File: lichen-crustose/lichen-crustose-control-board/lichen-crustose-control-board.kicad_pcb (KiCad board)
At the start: 4 copper layers, 48 x 108 mm, 77 parts, among them J1 Thonkiconn_Mono_Audio_Jack, J2 Thonkiconn_Mono_Audio_Jack, J3 Thonkiconn_Mono_Audio_Jack, J4 Thonkiconn_Mono_Audio_Jack, J5 Thonkiconn_Mono_Audio_Jack, J6 Thonkiconn_Mono_Audio_Jack, J7 Thonkiconn_Mono_Audio_Jack, J8 Thonkiconn_Mono_Audio_Jack, U1 NSL-32SR3, U2 NS-32SR2

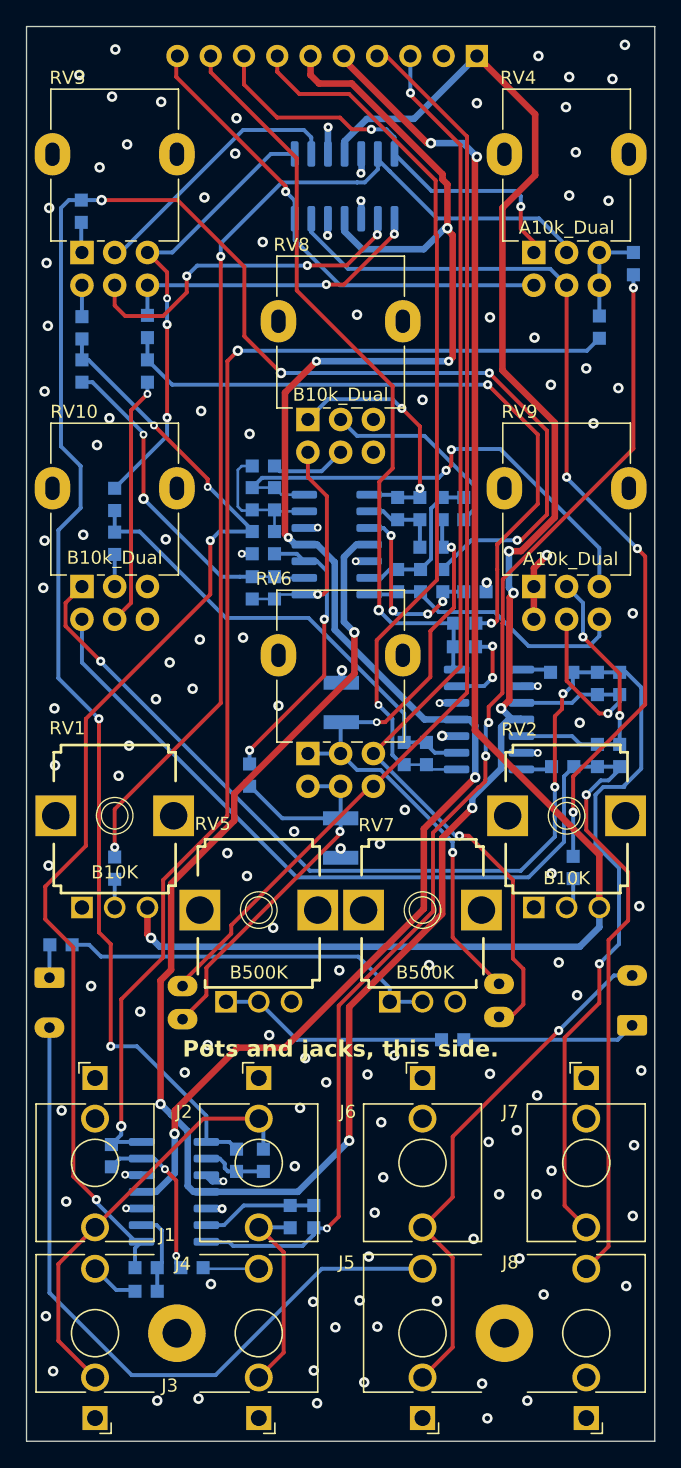
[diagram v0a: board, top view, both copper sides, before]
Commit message: Updates Lichen symbols and footprints. Fixes to Crustose and Vactrol VCA. Adds 3D model of the RP2350 dual USB board.
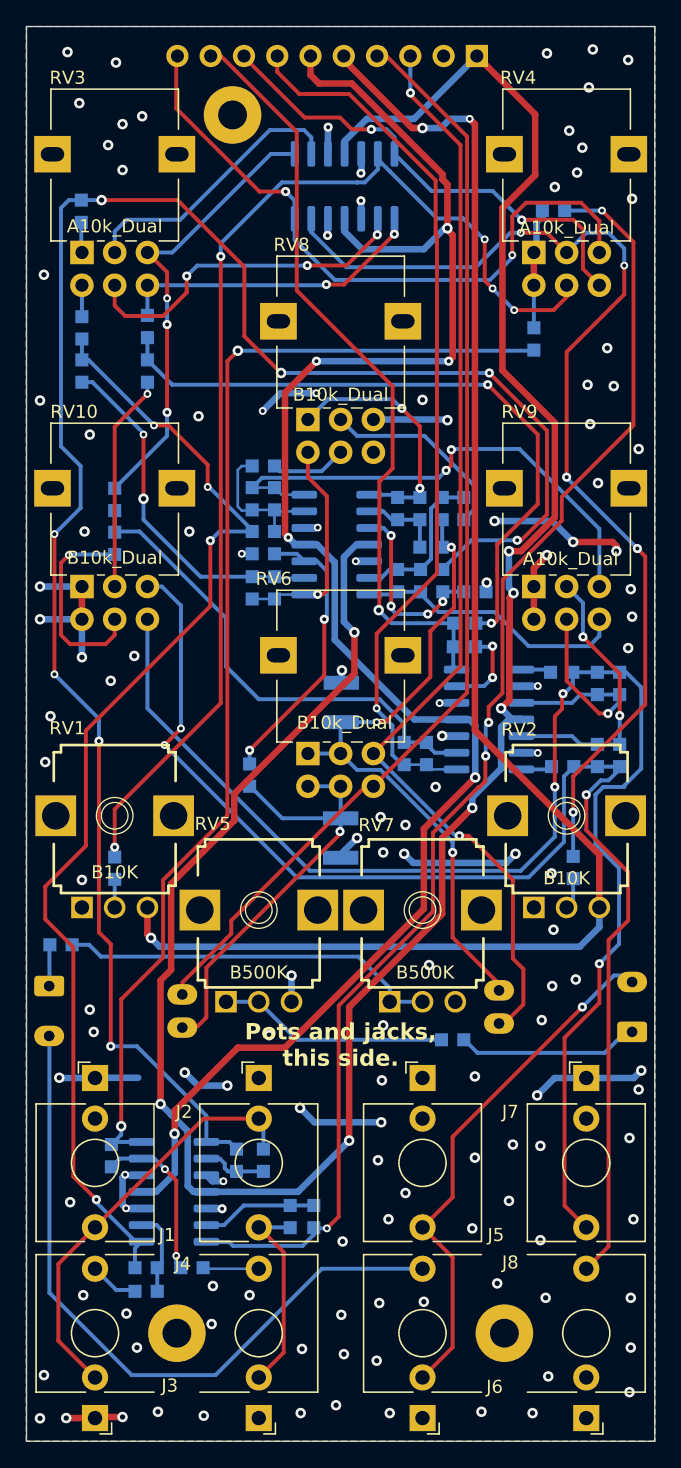
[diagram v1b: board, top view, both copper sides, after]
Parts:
- added H3: MountingHole_Pad, MountingHole:MountingHole_2.2mm_M2_Pad, F.Cu at (117.0, 117.0)
- R10, R13, R14: value 4.7k_0603 -> 5.1k_0603
- R11, R12, R35, R36, R37, R38, R39, R40: value 100k_0603 -> 10k_0603
- R15, R16, R33, R34: value 10k_0603 -> 1k_0603
- moved R13 7.32 mm to (141.5, 124.3), turned to 180 degrees
- moved R14 5.08 mm to (140.0, 134.1)
- moved U2 0.64 mm to (103.0, 183.5)
- moved U1 0.50 mm to (147.5, 187.0)
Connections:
- RV10 pad 1: /OUTPUT_FEEDBACK_L -> GND
- RV10 pad 2: /Amplifiers/FEEDBACK_MIX_L -> /Amplifiers/FEEDBACK_MIX_R
- RV10 pad 3: GND -> /OUTPUT_FEEDBACK_R
- RV10 pad 4: /OUTPUT_FEEDBACK_R -> GND
- RV10 pad 5: /Amplifiers/FEEDBACK_MIX_R -> /Amplifiers/FEEDBACK_MIX_L
- RV10 pad 6: GND -> /OUTPUT_FEEDBACK_L
- RV4 pad 1: /CARRER_CONNECTOR_L -> /Amplifiers/CARRIER_UNAMPLIFIED_L
- RV4 pad 2: /Amplifiers/CARRIER_AMPLIFICATION_L -> /Amplifiers/CARRER_AMPLIFICATION_R
- RV4 pad 3: /Amplifiers/CARRIER_UNAMPLIFIED_L -> /PROGRAM_CONNECTOR_R
- RV4 pad 4: /PROGRAM_CONNECTOR_R -> /Amplifiers/CARRIER_UNAMPLIFIED_L
- RV4 pad 5: /Amplifiers/CARRER_AMPLIFICATION_R -> /Amplifiers/CARRIER_AMPLIFICATION_L
- RV4 pad 6: /Amplifiers/CARRIER_UNAMPLIFIED_L -> /CARRER_CONNECTOR_L
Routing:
- net GND: track 26.9 -> 104.1 mm, vias 130 -> 134
- net /Amplifiers/FEEDBACK_MIX_L: track 2.45 -> 15.7 mm, vias 0 -> 1
- net /PROGRAM_CONNECTOR_R: track 37.5 -> 50.8 mm, vias 1 -> 2
- net /Amplifiers/CARRER_AMPLIFICATION_R: track 70.6 -> 81.8 mm, vias 3 -> 5
- net /Amplifiers/CARRIER_IN_L: track 92.8 -> 101.5 mm
- net /OUTPUT_FEEDBACK_L: track 115.6 -> 110.0 mm, vias 4 -> 3
- net /Amplifiers/CARRIER_IN_R: track 95.0 -> 89.6 mm
- net /Amplifiers/CARRIER_AMPLIFICATION_L: track 83.8 -> 88.5 mm, vias 2 -> 5
- net /CARRER_CONNECTOR_L: track 32.3 -> 36.9 mm
- net /Amplifiers/FEEDBACK_MIX_R: track 19.1 -> 16.6 mm
- net /OUTPUT_FEEDBACK_R: track 100.0 -> 102.2 mm, vias 1 -> 3
- net -2.5V: track 113.9 -> 115.7 mm
- net /Amplifiers/CARRIER_UNAMPLIFIED_L: track 7.45 -> 9.22 mm
- net Net-(OP4C--): track 36.1 -> 37.9 mm
- net /Crossfaders/FILTER_OUT_R: track 33.2 -> 34.5 mm
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- added copper zone on B.Cu, net GND
- added copper zone on F.Cu, net GND
- removed copper zone on In1.Cu, net GND
- removed copper zone on In2.Cu, net GND
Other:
- copper layers 4 -> 2
- board text added: "v1.1 © 2026, Colin Clark"
- board text removed: "v1.0 © 2025, Colin Clark"

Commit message: feat: Updates Crustose, Cladonia and YouMe Transformer. Adds Stereo Latencies.
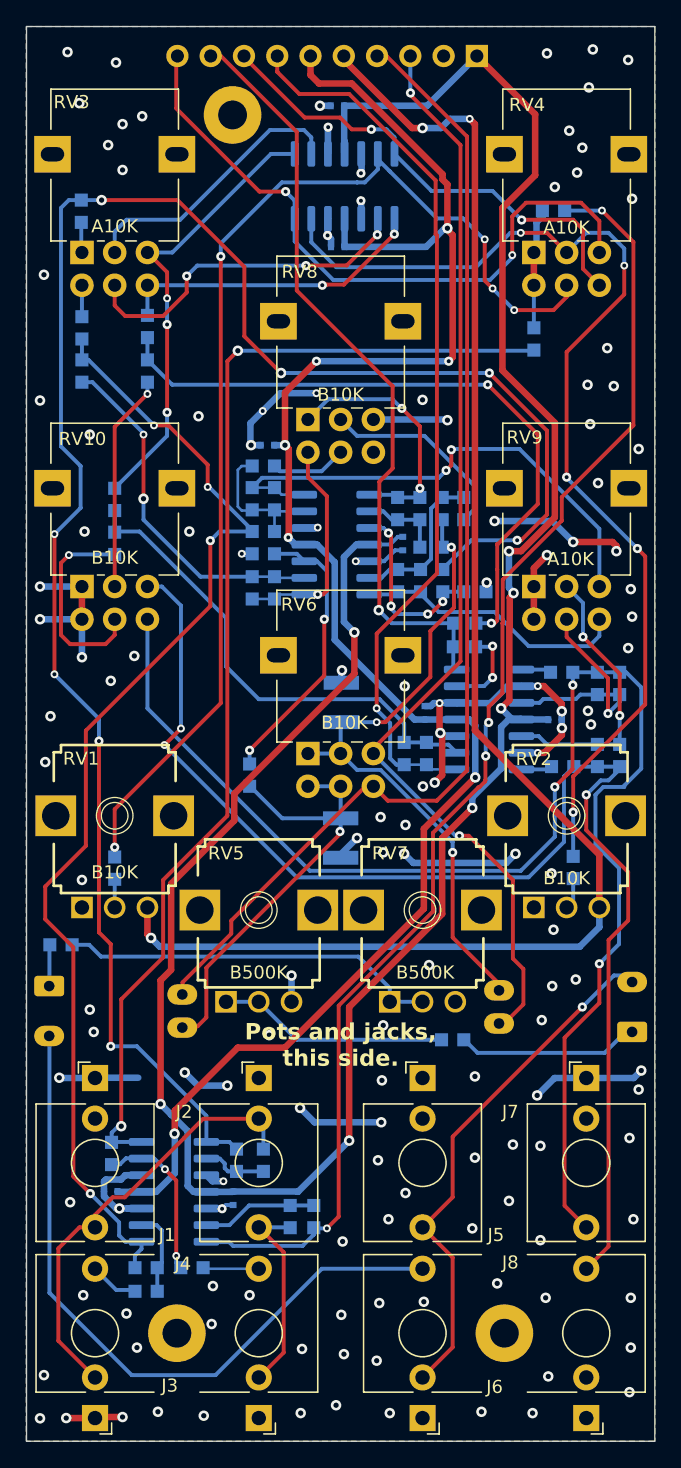
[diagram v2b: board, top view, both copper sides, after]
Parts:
- added C11: 100nF, RP2350_60QFN_minimal:C_0402_1005Metric_small_pads, B.Cu at (125.0, 116.3)
- added C12: 100nF, RP2350_60QFN_minimal:C_0402_1005Metric_small_pads, B.Cu at (141.6, 163.2)
- added C13: 100nF, RP2350_60QFN_minimal:C_0402_1005Metric_small_pads, B.Cu at (130.0, 149.7)
- added C14: 100nF, RP2350_60QFN_minimal:C_0402_1005Metric_small_pads, B.Cu at (117.0, 199.7)
- added C16: 100nF, RP2350_60QFN_minimal:C_0402_1005Metric_small_pads, B.Cu at (119.7, 142.2)
- added C17: 100nF, RP2350_60QFN_minimal:C_0402_1005Metric_small_pads, B.Cu at (107.7, 199.2)
- added C18: 100nF, RP2350_60QFN_minimal:C_0402_1005Metric_small_pads, B.Cu at (131.7, 162.6)
- added C19: 100nF, RP2350_60QFN_minimal:C_0402_1005Metric_small_pads, B.Cu at (125.0, 127.1)
- C3, C4, C5, C6: value 33pF_C0G_0603_50V -> 33pF C0G
- R1, R17, R18, R19, R2, R20, R21, R22, R23, R24, R25, R26, R27, R28, R29, R3, R30, R4, R5, R6, R7, R8: value 100k_0603 -> 100K
- R10, R13, R14, R9: value 5.1k_0603 -> 5.1K
- R11, R12, R31, R32, R35, R36, R37, R38, R39, R40: value 10k_0603 -> 10K
- R15, R16, R33, R34: value 1k_0603 -> 1K
- RV10, RV6, RV8: value B10k_Dual -> B10K
- RV3, RV4, RV9: value A10k_Dual -> A10K
- moved R8 0.17 mm to (107.8, 196.3)
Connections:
- net /Amplifiers/CARRER_AMPLIFICATION_R renamed /Amplifiers/CARRIER_OFFSET_R
- net /Amplifiers/CARRIER_AMPLIFICATION_L renamed /Amplifiers/CARRIER_OFFSET_L
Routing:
- net GND: track 104.1 -> 137.3 mm, vias 134 -> 141
- net +12V: track 182.7 -> 190.1 mm
- net /CONNECTOR_RM_R: track 84.3 -> 88.7 mm
- net -12V: track 137.3 -> 140.5 mm, vias 6 -> 7
- net PROGRAM_UNBUFFERED_L: track 32.2 -> 33.5 mm
